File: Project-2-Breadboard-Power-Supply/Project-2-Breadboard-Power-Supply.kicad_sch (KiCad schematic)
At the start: 17 parts, among them J1 Conn_01x02_Pin, J2 Conn_01x02_Pin, J3 Conn_01x03_Pin, J4 Conn_01x03_Pin, J5 Screw_Terminal_01x02, J6 Barrel_Jack_Switch, J7 Screw_Terminal_01x02, U1 LM7805_TO220, U2 LM317_TO-220

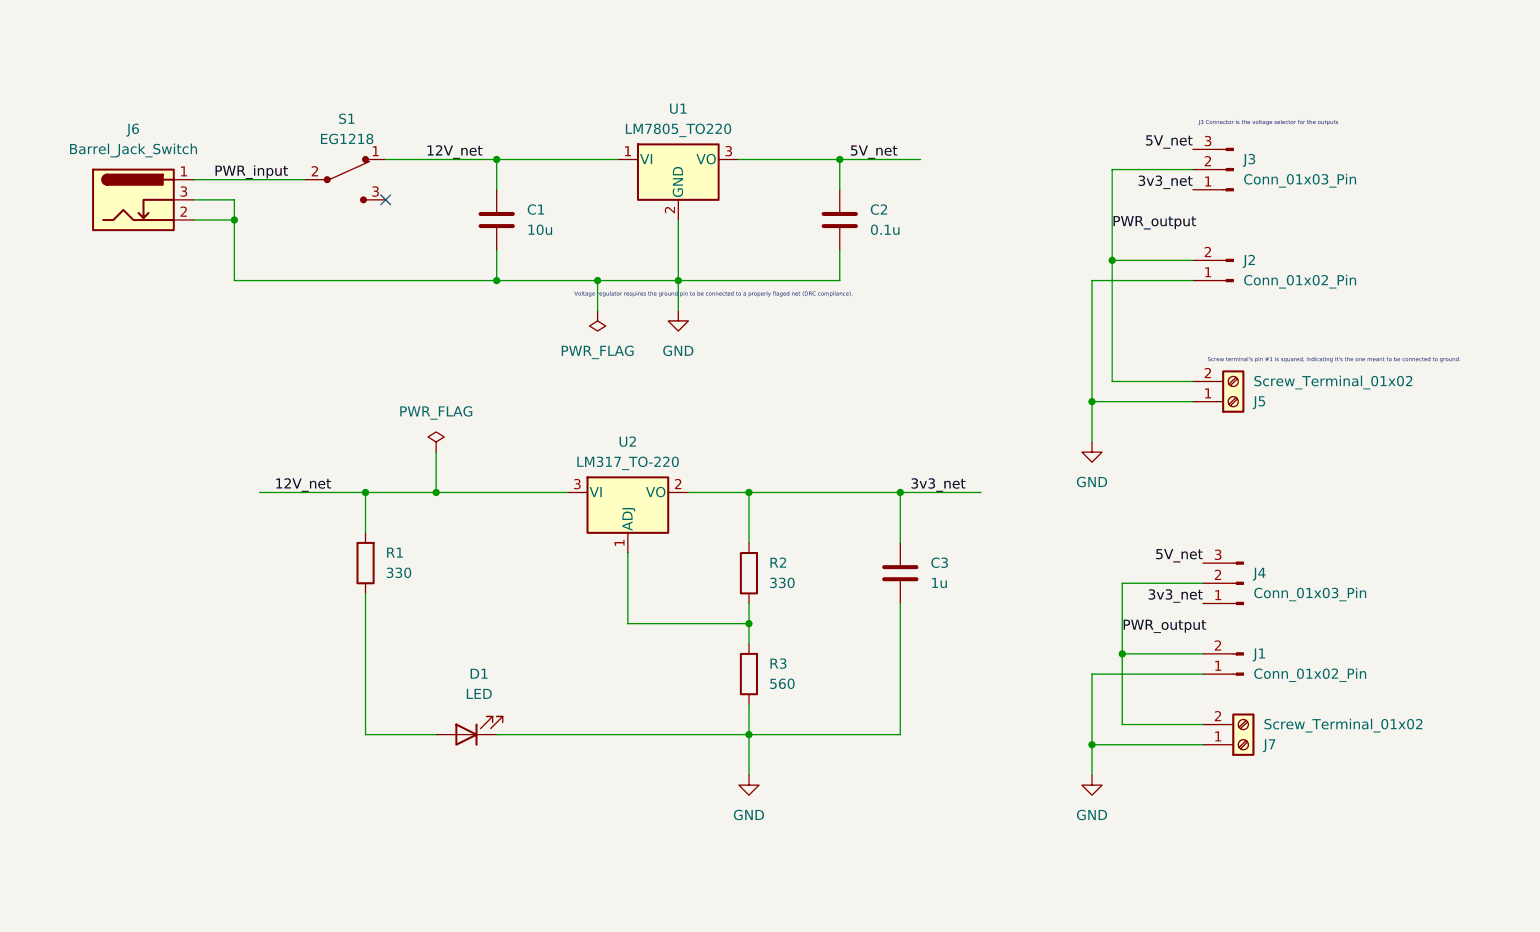
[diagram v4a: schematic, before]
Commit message: Add comments, boxes (step 7)
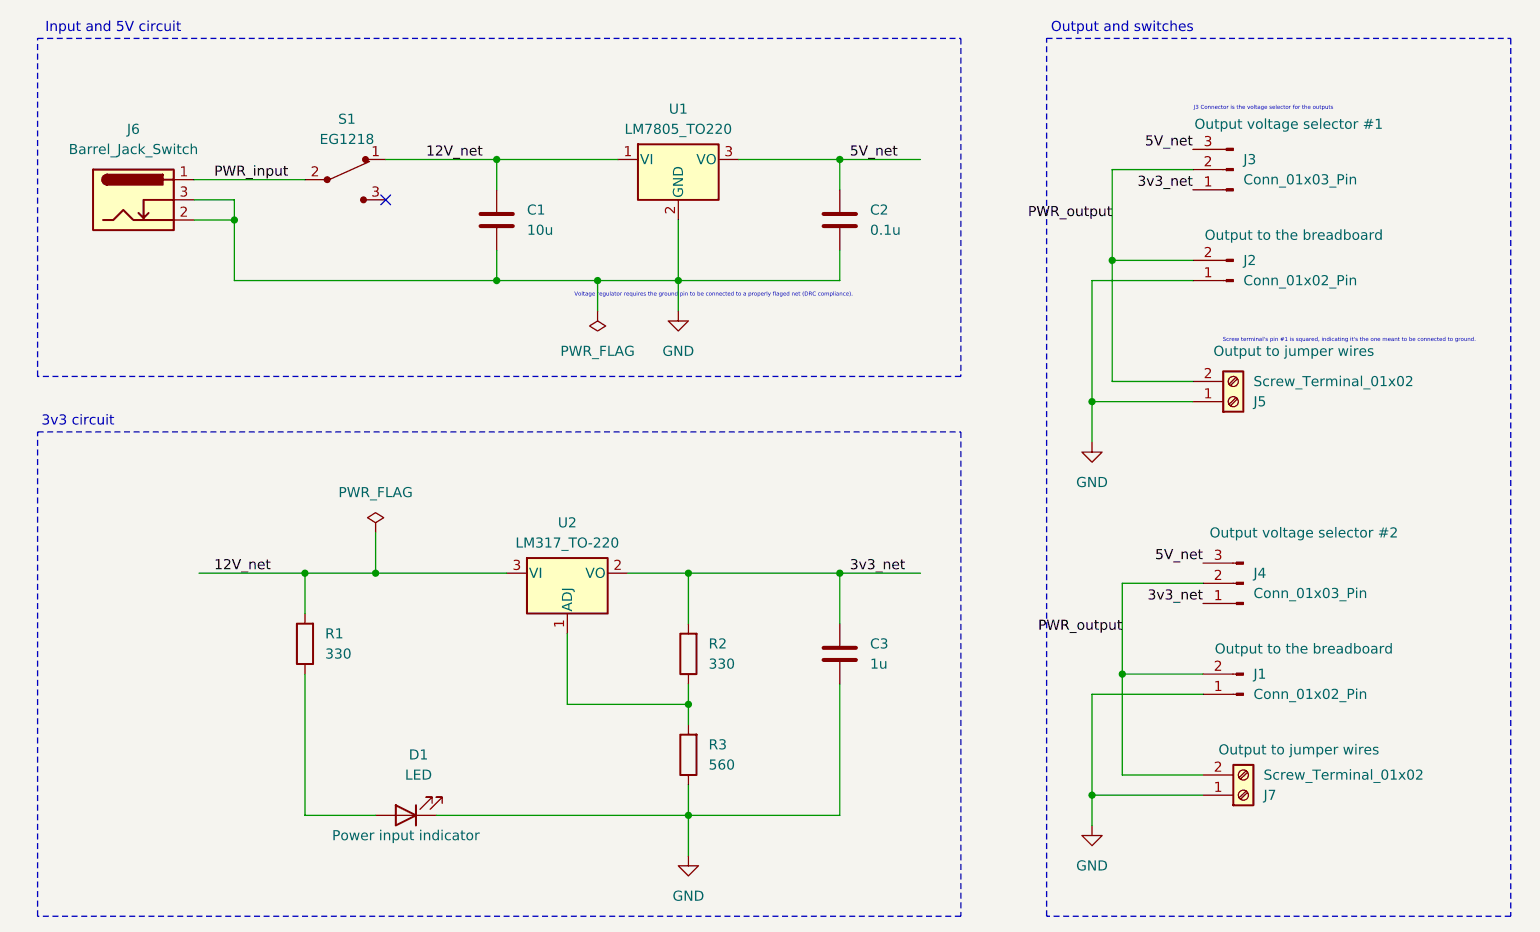
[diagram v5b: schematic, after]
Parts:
- D1: Purpose (none) -> Power input indicator
- J1, J2: Purpose (none) -> Output to the breadboard
- J3: Purpose (none) -> Output voltage selector #1
- J4: Purpose (none) -> Output voltage selector #2
- J5, J7: Purpose (none) -> Output to jumper wires
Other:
- note added: "3v3 circuit"
- note added: "Input and 5V circuit"
- note added: "Output and switches"
- moved on the sheet: C3, D1, J1, J7, R1, R2, R3, U2

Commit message: bugfix: add and assign missing library symbol and footprint
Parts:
- S1: footprint digikey-footprints:Switch_Slide_11.6x4mm_EG1218 -> Custom_Library_0.pretty:SW_1218_EWI
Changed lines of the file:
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@@
 			)
 		)
-		(property "Footprint" "digikey-footprints:Switch_Slide_11.6x4mm_EG1218"
+		(property "Footprint" "Custom_Library_0.pretty:SW_1218_EWI"
 			(at 69.85 33.02 0)
 			(hide yes)
@@
 			)
 		)
+		(property "Purpose" ""
+			(at 64.77 38.1 0)
+			(show_name no)
+			(do_not_autoplace no)
+			(effects
+				(font
+					(size 1.27 1.27)
+				)
+			)
+		)

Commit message: bugfix: segregate power output networks
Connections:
- net PWR_output renamed PWR_OUT_1
- net PWR_OUT_1: no longer J1.2 (Pin_2), J4.2 (Pin_2), J7.2 (Pin_2)
- new net PWR_OUT_2: J1.2 (Pin_2), J4.2 (Pin_2), J7.2 (Pin_2)
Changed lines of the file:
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@@
 		)
 	)
-	(label "PWR_output"
+	(label "PWR_OUT_1"
 		(at 161.29 43.18 180)
 		(fields_autoplaced yes)
@@
 		)
 	)
-	(label "PWR_output"
+	(label "PWR_OUT_2"
 		(at 162.56 95.25 180)
 		(fields_autoplaced yes)
